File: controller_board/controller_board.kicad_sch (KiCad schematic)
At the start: 9 parts, among them U1 NRF24L01_Breakout, U2 DEV-15583, U3 DM-OLED096-636, U4 TLV1117LV33DCYR

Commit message: adding gerber files
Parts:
- added J1: Conn_01x02_Pin, Connector_PinHeader_1.00mm:PinHeader_1x02_P1.00mm_Vertical, symbol Connector:Conn_01x02_Pin
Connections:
- net +3.3V: now also C1.1, U2.VIN, U4.2 (OUT_2)
- net +5V: now also J1.1 (Pin_1)
- net GND: now also J1.2 (Pin_2)
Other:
- moved on the sheet: C1, C2, U4

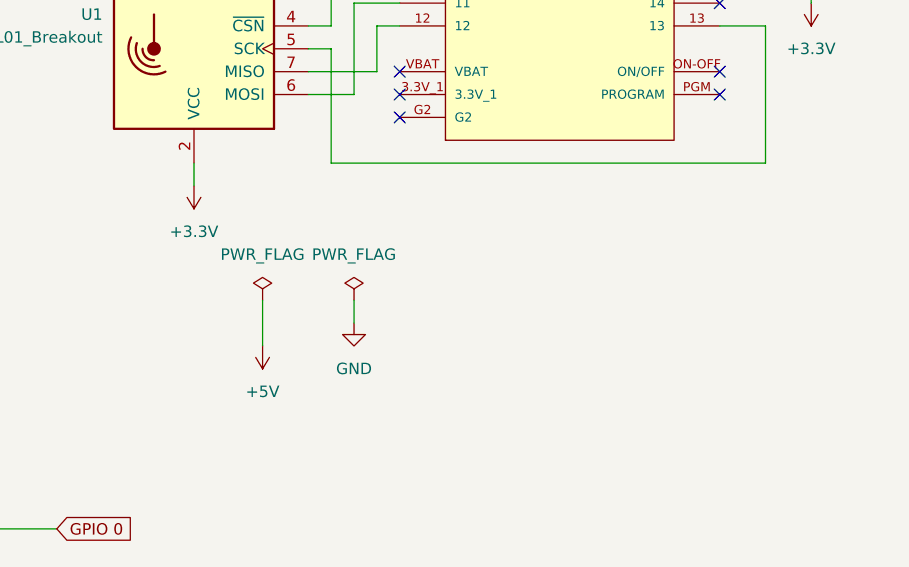
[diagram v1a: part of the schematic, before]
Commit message: added a capacitor to nrf24l01 module
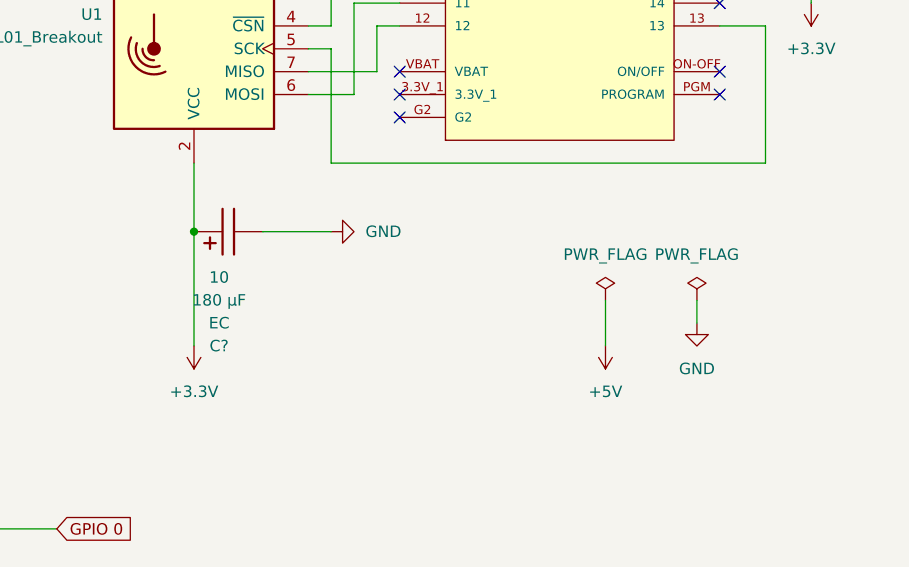
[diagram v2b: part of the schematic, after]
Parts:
- added C?: P2.5D6.3L11_860020273008, Capacitor_THT_Wurth:CP_Wurth_WCAP-ATG5-P2.5D6.3L11, symbol Electrolytic Capacitor:P2.5D6.3L11_860020273008
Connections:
- net +3.3V: now also C?.1
- net GND: now also C?.2

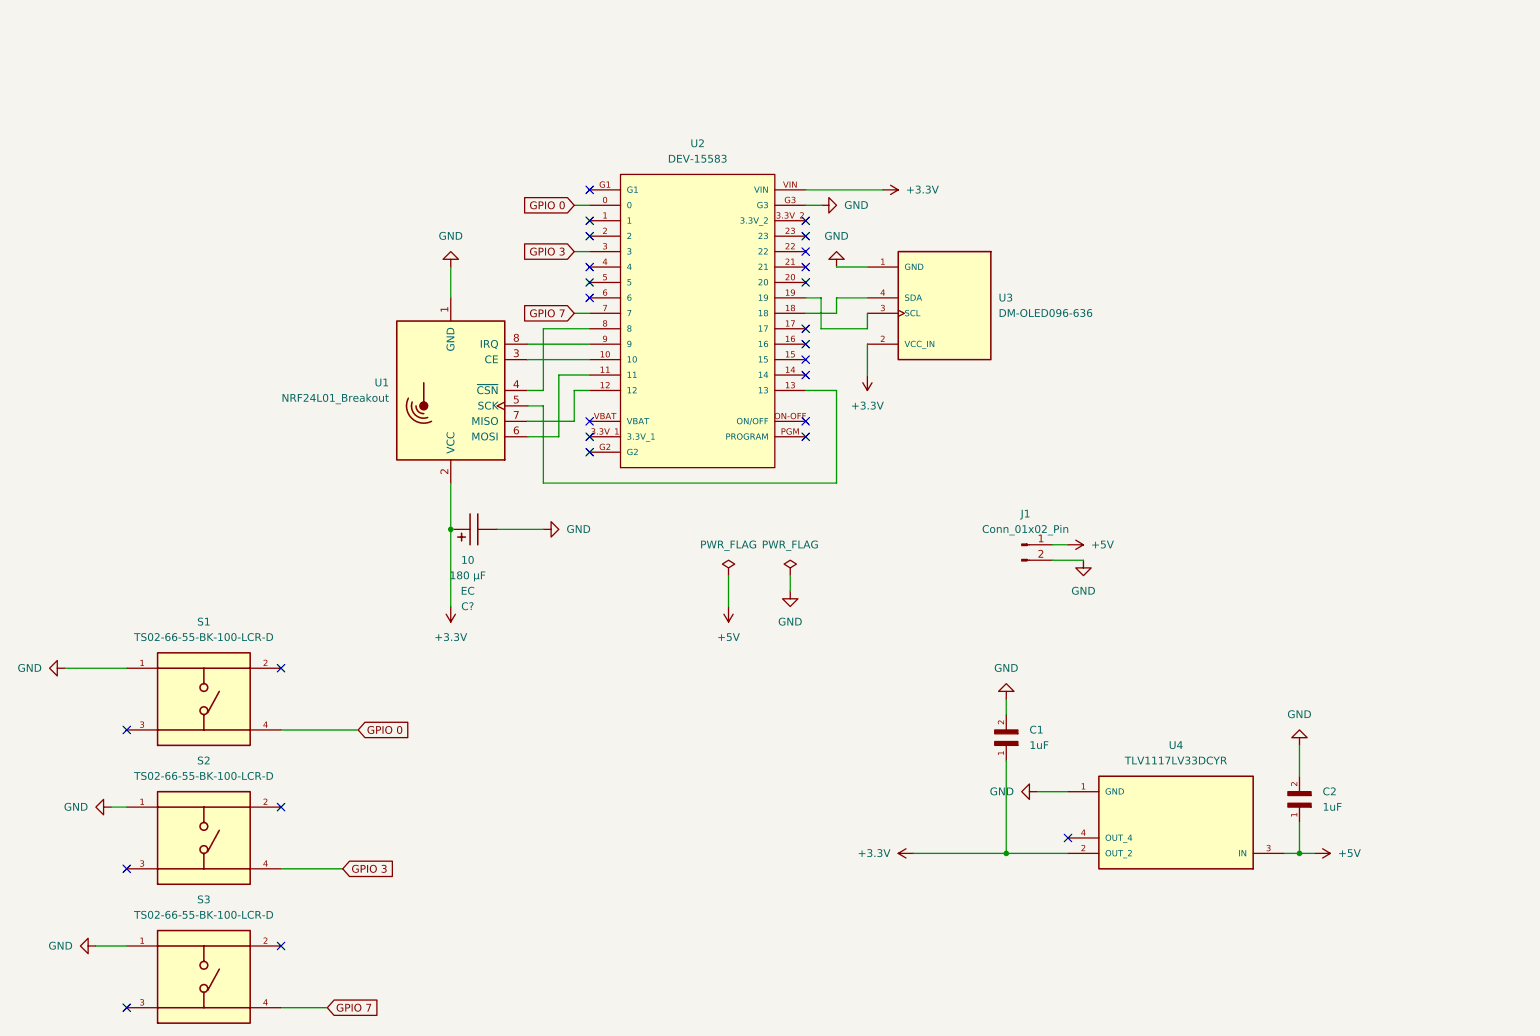
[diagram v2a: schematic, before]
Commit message: added case
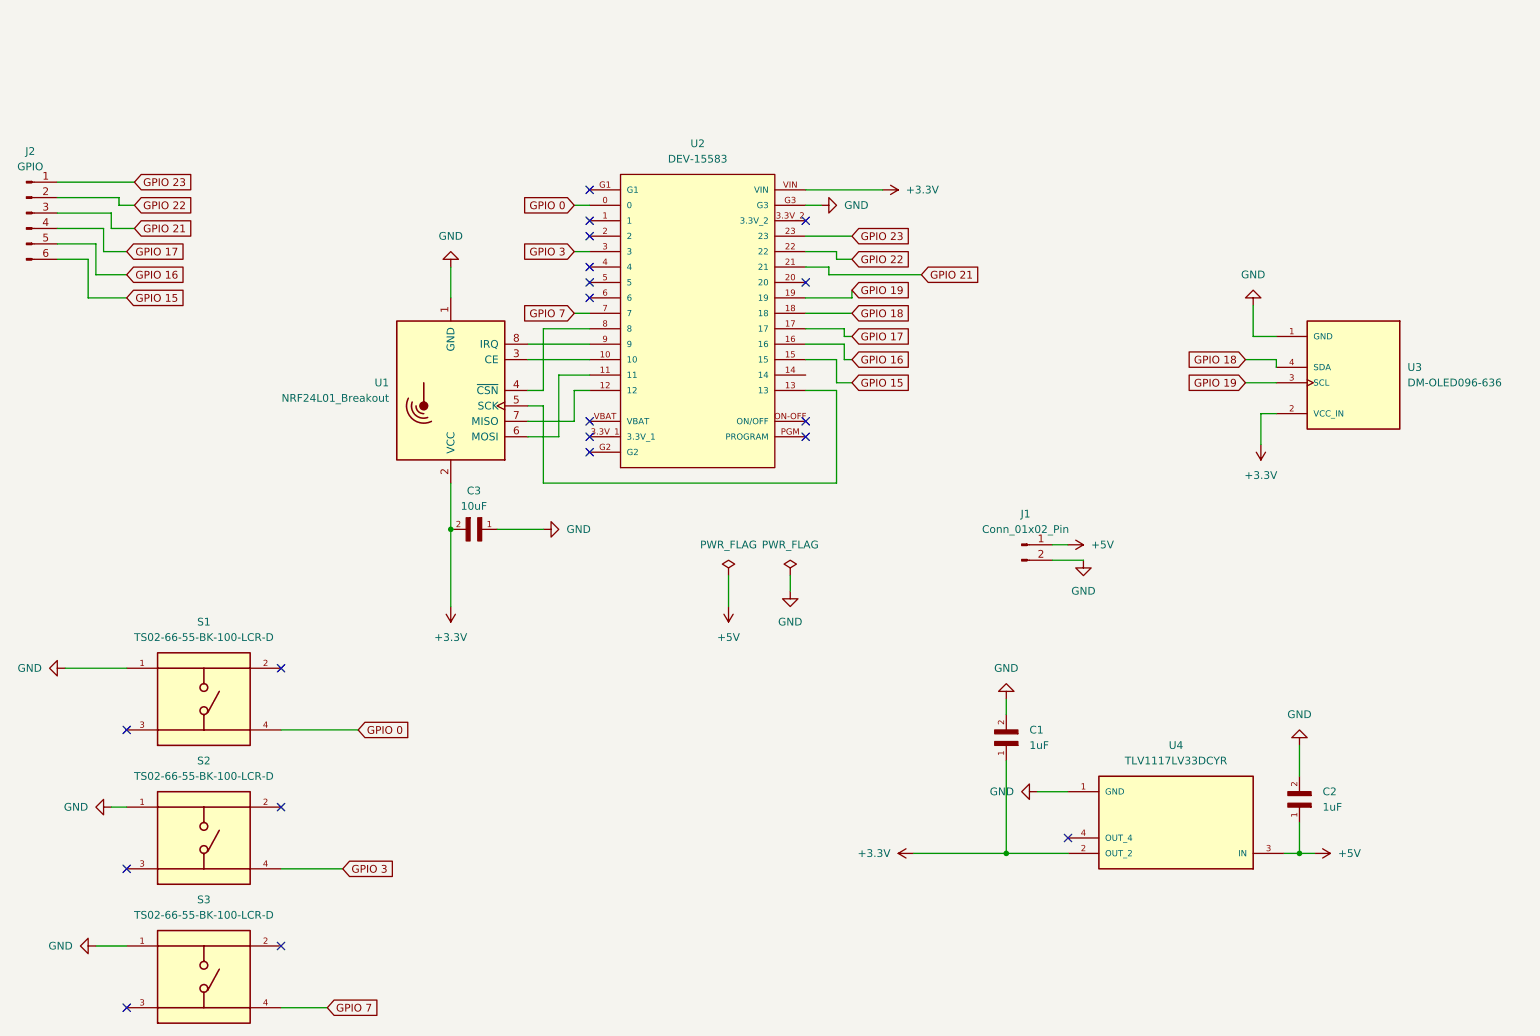
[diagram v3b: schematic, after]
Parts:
- removed C?: P2.5D6.3L11_860020273008, Capacitor_THT_Wurth:CP_Wurth_WCAP-ATG5-P2.5D6.3L11, symbol Electrolytic Capacitor:P2.5D6.3L11_860020273008
- added C3: 10uF, C0603C220J5GACTU:CAPC1608X87N, symbol C0603C223J5RACTU:C0603C223J5RACTU
- added J2: GPIO, Connector_PinHeader_1.00mm:PinHeader_1x06_P1.00mm_Vertical, symbol Connector:Conn_01x06_Pin
- C1: footprint C0603C223J5RACTU:CAPC1608X87N -> C0603C220J5GACTU:CAPC1608X87N
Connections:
- net +3.3V: now also C3.2
- net GND: now also C3.1
- net GPIO 15: now reaches U2.15
- net GPIO 15: now also J2.6 (Pin_6)
- net GPIO 16: now reaches U2.16
- net GPIO 16: now also J2.5 (Pin_5)
- net GPIO 17: now reaches U2.17
- net GPIO 17: now also J2.4 (Pin_4)
- net GPIO 18: now reaches U2.18, U3.4 (SDA)
- net GPIO 18: no longer U2.19, U3.3 (SCL)
- net GPIO 21: now reaches U2.21
- net GPIO 21: now also J2.3 (Pin_3)
- net GPIO 22: now reaches U2.22
- net GPIO 22: now also J2.2 (Pin_2)
- net GPIO 23: now reaches U2.23
- net GPIO 23: now also J2.1 (Pin_1)
- new net GPIO 19: U2.19, U3.3 (SCL)
- no-connect marks 27 -> 20

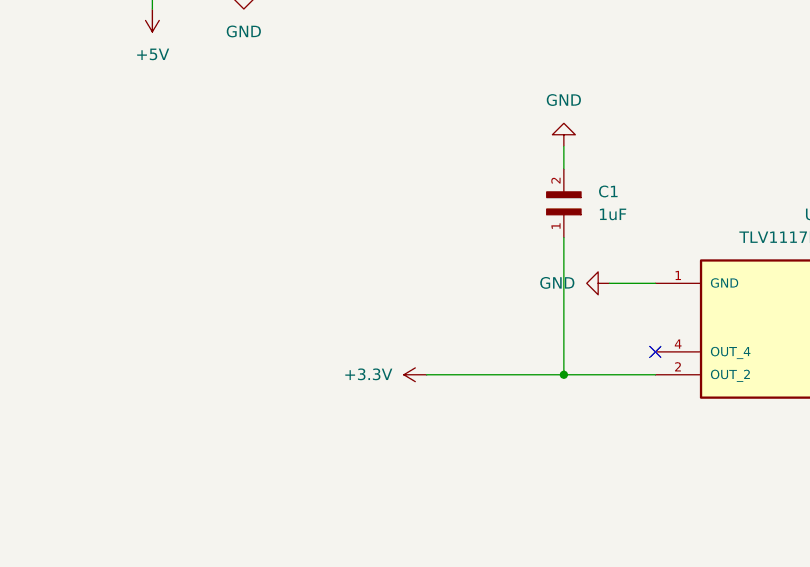
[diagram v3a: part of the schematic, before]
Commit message: added case and new images of ADS1293 breakout board and controller board case
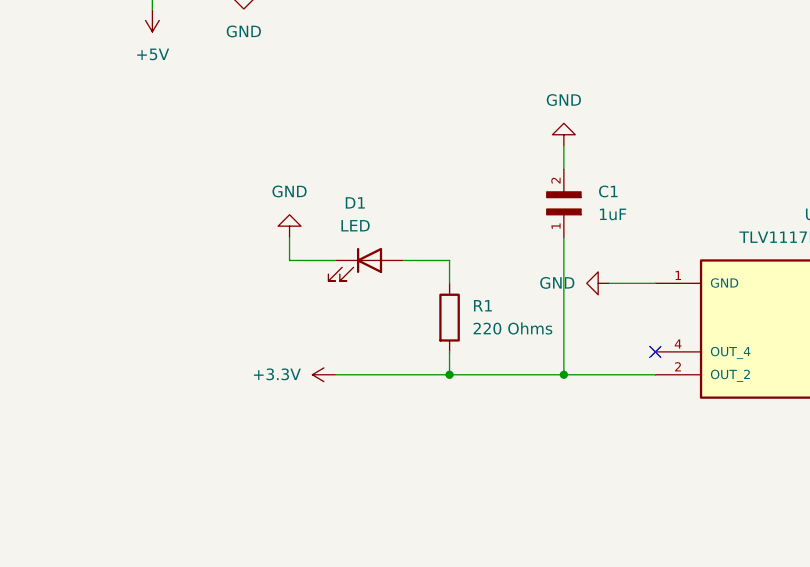
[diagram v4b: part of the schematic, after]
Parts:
- added D1: LED, LED_SMD:LED_0603_1608Metric_Pad1.05x0.95mm_HandSolder, symbol Device:LED
- added R1: 220 Ohms, Resistor_SMD:R_0603_1608Metric_Pad0.98x0.95mm_HandSolder, symbol Device:R
- J1: footprint Connector_PinHeader_1.00mm:PinHeader_1x02_P1.00mm_Vertical -> Connector_PinHeader_2.54mm:PinHeader_1x02_P2.54mm_Vertical
- J2: footprint Connector_PinHeader_1.00mm:PinHeader_1x06_P1.00mm_Vertical -> Connector_PinHeader_2.54mm:PinHeader_1x06_P2.54mm_Vertical
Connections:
- net +3.3V: now also R1.2
- net GND: now also D1.1 (K)
- new net: D1.2 (A), R1.1
